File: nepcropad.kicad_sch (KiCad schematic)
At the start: 34 parts, among them SW1 SW_Push, U1 ATmega32U4-A, Y1 16MHz

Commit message: PCB Layout
did the pcb layout
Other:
- moved on the sheet: D1, D2, D3, D4, D5, D6, D7, D8, D9, MX1, MX2, MX3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

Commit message: Finished routing
I think atleast.
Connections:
- net COL0: now also U1.30 (PB6)
- net COL1: now also U1.29 (PB5)
- net COL2: now also U1.28 (PB4)
- net ROW0: now also U1.26 (PD6)
- net ROW1: now also U1.27 (PD7)
- net ROW2: now also U1.31 (PC6)
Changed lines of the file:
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@@
+    )
+  )
+  (global_label "ROW1" (shape input) (at 104.14 119.38 0) (fields_autoplaced)
+    (effects (font (size 1.27 1.27)) (justify left))
+    (property "Intersheet References" "${INTERSHEET_REFS}" (id 0) (at 111.8145 119.3006 0)
+      (effects (font (size 1.27 1.27)) (justify left) hide)
+    )
+  )
+  (global_label "ROW2" (shape input) (at 104.14 93.98 0) (fields_autoplaced)
+    (effects (font (size 1.27 1.27)) (justify left))
+    (property "Intersheet References" "${INTERSHEET_REFS}" (id 0) (at 111.8145 93.9006 0)
+      (effects (font (size 1.27 1.27)) (justify left) hide)
     )
   )
@@
     (effects (font (size 1.27 1.27)) (justify left))
     (property "Intersheet References" "${INTERSHEET_REFS}" (id 0) (at 136.0655 35.6394 0)
+      (effects (font (size 1.27 1.27)) (justify left) hide)
+    )
+  )
+  (global_label "ROW0" (shape input) (at 104.14 116.84 0) (fields_autoplaced)
+    (effects (font (size 1.27 1.27)) (justify left))
+    (property "Intersheet References" "${INTERSHEET_REFS}" (id 0) (at 111.8145 116.7606 0)
       (effects (font (size 1.27 1.27)) (justify left) hide)
     )
@@
     )
   )
+  (global_label "COL2" (shape input) (at 104.14 81.28 0) (fields_autoplaced)
+    (effects (font (size 1.27 1.27)) (justify left))
+    (property "Intersheet References" "${INTERSHEET_REFS}" (id 0) (at 111.3912 81.2006 0)
+      (effects (font (size 1.27 1.27)) (justify left) hide)
+    )
+  )
+  (global_label "COL1" (shape input) (at 104.14 83.82 0) (fields_autoplaced)
+    (effects (font (size 1.27 1.27)) (justify left))
+    (property "Intersheet References" "${INTERSHEET_REFS}" (id 0) (at 111.3912 83.7406 0)
+      (effects (font (size 1.27 1.27)) (justify left) hide)
+    )
+  )
   (global_label "ROW2" (shape input) (at 166.37 114.3 180) (fields_autoplaced)
     (effects (font (size 1.27 1.27)) (justify right))
@@
       (effects (font (size 1.27 1.27)) (justify left) hide)
     )
+  )
+  (global_label "COL0" (shape input) (at 104.14 86.36 0) (fields_autoplaced)
+    (effects (font (size 1.27 1.27)) (justify left))
+    (property "Intersheet References" "${INTERSHEET_REFS}" (id 0) (at 111.3912 86.2806 0)
+      (effects (font (size 1.27 1.27)) (justify left) hide)
+    )

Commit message: minimize pcb
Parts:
- removed USB1: Molex-0548190589, random-keyboard-parts:Molex-0548190589, symbol random-keyboard-parts:Molex-0548190589
- added J1: USB_C_Receptacle_USB2.0, usbc:USB_C_GCT_USB4085, symbol symbols:USB_C_Receptacle_USB2.0
- added R5, R6: 5.1k, resistor:R_0805_2012Metric, symbol device:R_Small
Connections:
- net COL0: now also U1.31 (PC6); no longer U1.30 (PB6)
- net COL1: now also U1.30 (PB6); no longer U1.29 (PB5)
- net D+: now also J1.A6 (D+), J1.B6 (D+)
- net D-: now also J1.A7 (D-), J1.B7 (D-)
- net GND: now also J1.A1 (GND), J1.A12 (GND), J1.B1 (GND), J1.B12 (GND), J1.S1 (SHIELD), R5.2, R6.2
- net ROW2: now also U1.29 (PB5); no longer U1.31 (PC6)
- net VCC: now also J1.A4 (VBUS), J1.A9 (VBUS), J1.B4 (VBUS), J1.B9 (VBUS)
- new net: J1.A5 (CC1), R5.1
- new net: J1.B5 (CC2), R6.1
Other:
- moved on the sheet: F1

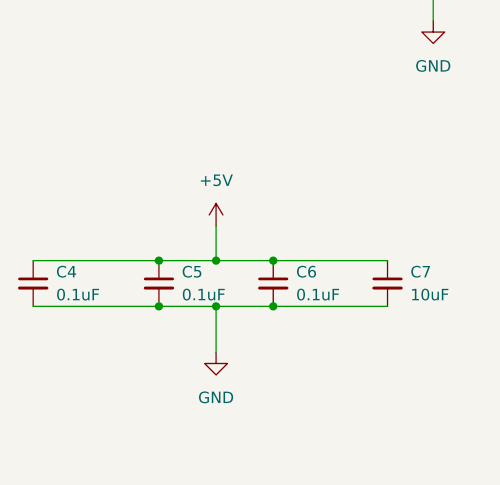
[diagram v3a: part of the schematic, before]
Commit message: update cap positions
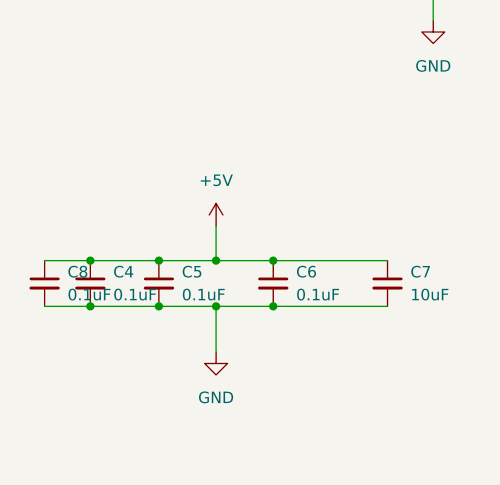
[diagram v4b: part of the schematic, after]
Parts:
- added C8: 0.1uF, Capacitor_SMD:C_0805_2012Metric, symbol Device:C_Small
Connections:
- net +5V: now also C8.1
- net GND: now also C8.2
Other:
- moved on the sheet: C4
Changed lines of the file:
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@@
   (junction (at 44.45 148.59) (diameter 0) (color 0 0 0 0)
   )
+  (junction (at 24.13 148.59) (diameter 0) (color 0 0 0 0)
+  )
   (junction (at 31.75 143.51) (diameter 0) (color 0 0 0 0)
   )
@@
   (junction (at 52.07 81.28) (diameter 0) (color 0 0 0 0)
   )
+  (junction (at 24.13 143.51) (diameter 0) (color 0 0 0 0)
+  )
   (junction (at 199.39 95.25) (diameter 0) (color 0 0 0 0)
   )
@@
     (stroke (width 0) (type default) (color 0 0 0 0))
   )
+  (wire (pts (xy 24.13 143.51) (xy 31.75 143.51))
+    (stroke (width 0) (type default) (color 0 0 0 0))
+  )
   (wire (pts (xy 199.39 71.12) (xy 204.47 71.12))
     (stroke (width 0) (type default) (color 0 0 0 0))
@@
     (stroke (width 0) (type default) (color 0 0 0 0))
   )
-  (wire (pts (xy 17.78 143.51) (xy 31.75 143.51))
+  (wire (pts (xy 19.05 143.51) (xy 24.13 143.51))
     (stroke (width 0) (type default) (color 0 0 0 0))
   )
@@
     (stroke (width 0) (type default) (color 0 0 0 0))
   )
+  (wire (pts (xy 24.13 148.59) (xy 31.75 148.59))
+    (stroke (width 0) (type default) (color 0 0 0 0))
+  )
   (wire (pts (xy 111.76 60.96) (xy 119.38 60.96))
     (stroke (width 0) (type default) (color 0 0 0 0))
@@
     (stroke (width 0) (type default) (color 0 0 0 0))
   )
-  (wire (pts (xy 17.78 148.59) (xy 31.75 148.59))
+  (wire (pts (xy 19.05 148.59) (xy 24.13 148.59))
     (stroke (width 0) (type default) (color 0 0 0 0))
   )
@@
     )
   )
+  (symbol (lib_id "Device:C_Small") (at 19.05 146.05 0) (unit 1)
+    (in_bom yes) (on_board yes) (fields_autoplaced)
+    (property "Reference" "C8" (id 0) (at 21.59 144.7862 0)
+      (effects (font (size 1.27 1.27)) (justify left))
+    )
+    (property "Value" "0.1uF" (id 1) (at 21.59 147.3262 0)
+      (effects (font (size 1.27 1.27)) (justify left))
+    )
+    (property "Footprint" "Capacitor_SMD:C_0805_2012Metric" (id 2) (at 19.05 146.05 0)
+      (effects (font (size 1.27 1.27)) hide)
+    )
+    (property "Datasheet" "~" (id 3) (at 19.05 146.05 0)
+      (effects (font (size 1.27 1.27)) hide)
+    )
+    (pin "1")
+    (pin "2")
+  )
   (symbol (lib_id "power:GND") (at 62.23 116.84 0) (unit 1)
     (in_bom yes) (on_board yes) (fields_autoplaced)
@@
     (pin "1")
   )
-  (symbol (lib_id "Device:C_Small") (at 17.78 146.05 0) (unit 1)
-    (in_bom yes) (on_board yes) (fields_autoplaced)
-    (property "Reference" "C4" (id 0) (at 20.32 144.7862 0)
-      (effects (font (size 1.27 1.27)) (justify left))
-    )
-    (property "Value" "0.1uF" (id 1) (at 20.32 147.3262 0)
-      (effects (font (size 1.27 1.27)) (justify left))
-    )
-    (property "Footprint" "Capacitor_SMD:C_0805_2012Metric" (id 2) (at 17.78 146.05 0)
-      (effects (font (size 1.27 1.27)) hide)
-    )
-    (property "Datasheet" "~" (id 3) (at 17.78 146.05 0)
+  (symbol (lib_id "Device:C_Small") (at 24.13 146.05 0) (unit 1)
+    (in_bom yes) (on_board yes) (fields_autoplaced)
+    (property "Reference" "C4" (id 0) (at 26.67 144.7862 0)
+      (effects (font (size 1.27 1.27)) (justify left))
+    )
+    (property "Value" "0.1uF" (id 1) (at 26.67 147.3262 0)
+      (effects (font (size 1.27 1.27)) (justify left))
+    )
+    (property "Footprint" "Capacitor_SMD:C_0805_2012Metric" (id 2) (at 24.13 146.05 0)
+      (effects (font (size 1.27 1.27)) hide)
+    )
+    (property "Datasheet" "~" (id 3) (at 24.13 146.05 0)
       (effects (font (size 1.27 1.27)) hide)
     )
@@
       (reference "C7") (unit 1) (value "10uF") (footprint "Capacitor_SMD:C_0805_2012Metric")
     )
+    (path "/04a095c3-3af8-4398-b3ce-c900a3aad31d"
+      (reference "C8") (unit 1) (value "0.1uF") (footprint "Capacitor_SMD:C_0805_2012Metric")
+    )
     (path "/0ba50094-50cb-4fb4-b09b-eb72c321b67c"

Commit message: Should be ready for placing an order
Added CPL and BOM

Changed out the USB-C connector as the original one we used is nolonger in production.
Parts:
- J1: footprint usbc:USB_C_GCT_USB4085 -> jlcusbc:TYPE-C-31-M-12
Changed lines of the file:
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@@
     (property "Reference" "J1" (id 0) (at 119.38 15.24 0))
     (property "Value" "USB_C_Receptacle_USB2.0" (id 1) (at 119.38 17.78 0))
-    (property "Footprint" "usbc:USB_C_GCT_USB4085" (id 2) (at 123.19 38.1 0)
+    (property "Footprint" "jlcusbc:TYPE-C-31-M-12" (id 2) (at 123.19 38.1 0)
       (effects (font (size 1.27 1.27)) hide)
     )
@@
     )
     (path "/a5342b95-2ea5-45aa-9992-cd7273a981fb"
-      (reference "J1") (unit 1) (value "USB_C_Receptacle_USB2.0") (footprint "usbc:USB_C_GCT_USB4085")
+      (reference "J1") (unit 1) (value "USB_C_Receptacle_USB2.0") (footprint "jlcusbc:TYPE-C-31-M-12")
     )
     (path "/a9e6ce0a-37dc-4fb3-b1ba-bf394a4f484c"

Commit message: MCU Footprint wrong for new MCU
I was about to checkout and noticed on the manufacturer's site that the MCU was a different size than the footprint used.

ATmega32U4-MUR smaller than AU version
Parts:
- U1: footprint Package_QFP:TQFP-44_10x10mm_P0.8mm -> ATmega32U4-MU:QFN44G-0.5-7X7MM
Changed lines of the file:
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@@
       (effects (font (size 1.27 1.27)) (justify left))
     )
-    (property "Footprint" "Package_QFP:TQFP-44_10x10mm_P0.8mm" (id 2) (at 88.9 109.22 0)
+    (property "Footprint" "ATmega32U4-MU:QFN44G-0.5-7X7MM" (id 2) (at 88.9 109.22 0)
       (effects (font (size 1.27 1.27) italic) hide)
     )
@@
     )
     (path "/db794584-6c7e-4806-a1b1-36b618523305"
-      (reference "U1") (unit 1) (value "ATmega32U4-A") (footprint "Package_QFP:TQFP-44_10x10mm_P0.8mm")
+      (reference "U1") (unit 1) (value "ATmega32U4-A") (footprint "ATmega32U4-MU:QFN44G-0.5-7X7MM")
     )
     (path "/8a0114f1-58f2-4045-ae75-3bf5f22bbf5e"
